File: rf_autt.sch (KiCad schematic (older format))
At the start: 10 parts

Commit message: PCB is Done... Needs DRC check
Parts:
- gave numbers to parts that had none: 10
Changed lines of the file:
@@
 $Descr A4 11693 8268
 encoding utf-8
-Sheet 7 14
+Sheet 7 7
 Title "HF-SDR RF-Attenuator"
 Date "2020 december"
@@
 OUT
 $Comp
-L sdr:FST3253 U?
+L sdr:FST3253 U4
 U 1 1 5FE50A6B
 P 5600 1900
-F 0 "U?" H 5350 2550 50  0000 C CNN
+F 0 "U4" H 5350 2550 50  0000 C CNN
 F 1 "FST3253" H 5800 2550 50  0000 C CNN
 F 2 "Package_SO:TSSOP-16_4.4x5mm_P0.65mm" H 5600 1900 50  0001 C CNN
@@
 ATT_SEL1
 $Comp
-L power:GNDA #PWR?
+L power:GNDA #PWR031
 U 1 1 5FE53082
 P 5600 4400
-F 0 "#PWR?" H 5600 4150 50  0001 C CNN
+F 0 "#PWR031" H 5600 4150 50  0001 C CNN
 F 1 "GNDA" H 5605 4227 50  0000 C CNN
 F 2 "" H 5600 4400 50  0001 C CNN
@@
 $EndComp
 $Comp
-L Device:R R?
+L Device:R R37
 U 1 1 5FE56E4E
 P 5600 4250
-F 0 "R?" H 5530 4204 50  0000 R CNN
+F 0 "R37" H 5530 4204 50  0000 R CNN
 F 1 "33" H 5530 4295 50  0000 R CNN
 F 2 "Resistor_SMD:R_0805_2012Metric_Pad1.20x1.40mm_HandSolder" V 5530 4250 50  0001 C CNN
@@
 $EndComp
 $Comp
-L Device:R R?
+L Device:R R24
 U 1 1 5FE5744A
 P 5300 3950
-F 0 "R?" V 5093 3950 50  0000 C CNN
+F 0 "R24" V 5093 3950 50  0000 C CNN
 F 1 "27" V 5184 3950 50  0000 C CNN
 F 2 "Resistor_SMD:R_0805_2012Metric_Pad1.20x1.40mm_HandSolder" V 5230 3950 50  0001 C CNN
@@
 $EndComp
 $Comp
-L Device:R R?
+L Device:R R40
 U 1 1 5FE57E99
 P 5900 3950
-F 0 "R?" V 5693 3950 50  0000 C CNN
+F 0 "R40" V 5693 3950 50  0000 C CNN
 F 1 "27" V 5784 3950 50  0000 C CNN
 F 2 "Resistor_SMD:R_0805_2012Metric_Pad1.20x1.40mm_HandSolder" V 5830 3950 50  0001 C CNN
@@
 	5600 3950 5750 3950
 $Comp
-L power:GNDA #PWR?
+L power:GNDA #PWR033
 U 1 1 5FE5C53B
 P 5600 6600
-F 0 "#PWR?" H 5600 6350 50  0001 C CNN
+F 0 "#PWR033" H 5600 6350 50  0001 C CNN
 F 1 "GNDA" H 5605 6427 50  0000 C CNN
 F 2 "" H 5600 6600 50  0001 C CNN
@@
 $EndComp
 $Comp
-L Device:R R?
+L Device:R R39
 U 1 1 5FE5C541
 P 5600 6450
-F 0 "R?" H 5530 6404 50  0000 R CNN
+F 0 "R39" H 5530 6404 50  0000 R CNN
 F 1 "3" H 5530 6495 50  0000 R CNN
 F 2 "Resistor_SMD:R_0805_2012Metric_Pad1.20x1.40mm_HandSolder" V 5530 6450 50  0001 C CNN
@@
 $EndComp
 $Comp
-L Device:R R?
+L Device:R R36
 U 1 1 5FE5C547
 P 5300 6150
-F 0 "R?" V 5093 6150 50  0000 C CNN
+F 0 "R36" V 5093 6150 50  0000 C CNN
 F 1 "47" V 5184 6150 50  0000 C CNN
 F 2 "Resistor_SMD:R_0805_2012Metric_Pad1.20x1.40mm_HandSolder" V 5230 6150 50  0001 C CNN
@@
 $EndComp
 $Comp
-L Device:R R?
+L Device:R R42
 U 1 1 5FE5C54D
 P 5900 6150
-F 0 "R?" V 5693 6150 50  0000 C CNN
+F 0 "R42" V 5693 6150 50  0000 C CNN
 F 1 "47" V 5784 6150 50  0000 C CNN
 F 2 "Resistor_SMD:R_0805_2012Metric_Pad1.20x1.40mm_HandSolder" V 5830 6150 50  0001 C CNN
@@
 	5600 6150 5750 6150
 $Comp
-L power:GNDA #PWR?
+L power:GNDA #PWR032
 U 1 1 5FE5CA2D
 P 5600 5500
-F 0 "#PWR?" H 5600 5250 50  0001 C CNN
+F 0 "#PWR032" H 5600 5250 50  0001 C CNN
 F 1 "GNDA" H 5605 5327 50  0000 C CNN
 F 2 "" H 5600 5500 50  0001 C CNN
@@
 $EndComp
 $Comp
-L Device:R R?
+L Device:R R38
 U 1 1 5FE5CA33
 P 5600 5350
-F 0 "R?" H 5530 5304 50  0000 R CNN
+F 0 "R38" H 5530 5304 50  0000 R CNN
 F 1 "10" H 5530 5395 50  0000 R CNN
 F 2 "Resistor_SMD:R_0805_2012Metric_Pad1.20x1.40mm_HandSolder" V 5530 5350 50  0001 C CNN
@@
 $EndComp
 $Comp
-L Device:R R?
+L Device:R R35
 U 1 1 5FE5CA39
 P 5300 5050
-F 0 "R?" V 5093 5050 50  0000 C CNN
+F 0 "R35" V 5093 5050 50  0000 C CNN
 F 1 "39" V 5184 5050 50  0000 C CNN
 F 2 "Resistor_SMD:R_0805_2012Metric_Pad1.20x1.40mm_HandSolder" V 5230 5050 50  0001 C CNN
@@
 $EndComp
 $Comp
-L Device:R R?
+L Device:R R41
 U 1 1 5FE5CA3F
 P 5900 5050
-F 0 "R?" V 5693 5050 50  0000 C CNN
+F 0 "R41" V 5693 5050 50  0000 C CNN
 F 1 "39" V 5784 5050 50  0000 C CNN
 F 2 "Resistor_SMD:R_0805_2012Metric_Pad1.20x1.40mm_HandSolder" V 5830 5050 50  0001 C CNN
@@
 	4300 800  5100 800
 $Comp
-L power:GNDA #PWR?
+L power:GNDA #PWR030
 U 1 1 5FF9D7B5
 P 5600 2700
-F 0 "#PWR?" H 5600 2450 50  0001 C CNN
+F 0 "#PWR030" H 5600 2450 50  0001 C CNN
 F 1 "GNDA" H 5605 2527 50  0000 C CNN
 F 2 "" H 5600 2700 50  0001 C CNN
@@
 $EndComp
 $Comp
-L power:GNDA #PWR?
+L power:GNDA #PWR034
 U 1 1 5FF9DC72
 P 6300 1550
-F 0 "#PWR?" H 6300 1300 50  0001 C CNN
+F 0 "#PWR034" H 6300 1300 50  0001 C CNN
 F 1 "GNDA" H 6305 1377 50  0000 C CNN
 F 2 "" H 6300 1550 50  0001 C CNN
@@
 Connection ~ 6300 1550
 $Comp
-L power:+5VA #PWR?
+L power:+5VA #PWR029
 U 1 1 5FF9E701
 P 5600 1200
-F 0 "#PWR?" H 5600 1050 50  0001 C CNN
+F 0 "#PWR029" H 5600 1050 50  0001 C CNN
 F 1 "+5VA" H 5615 1373 50  0000 C CNN
 F 2 "" H 5600 1200 50  0001 C CNN

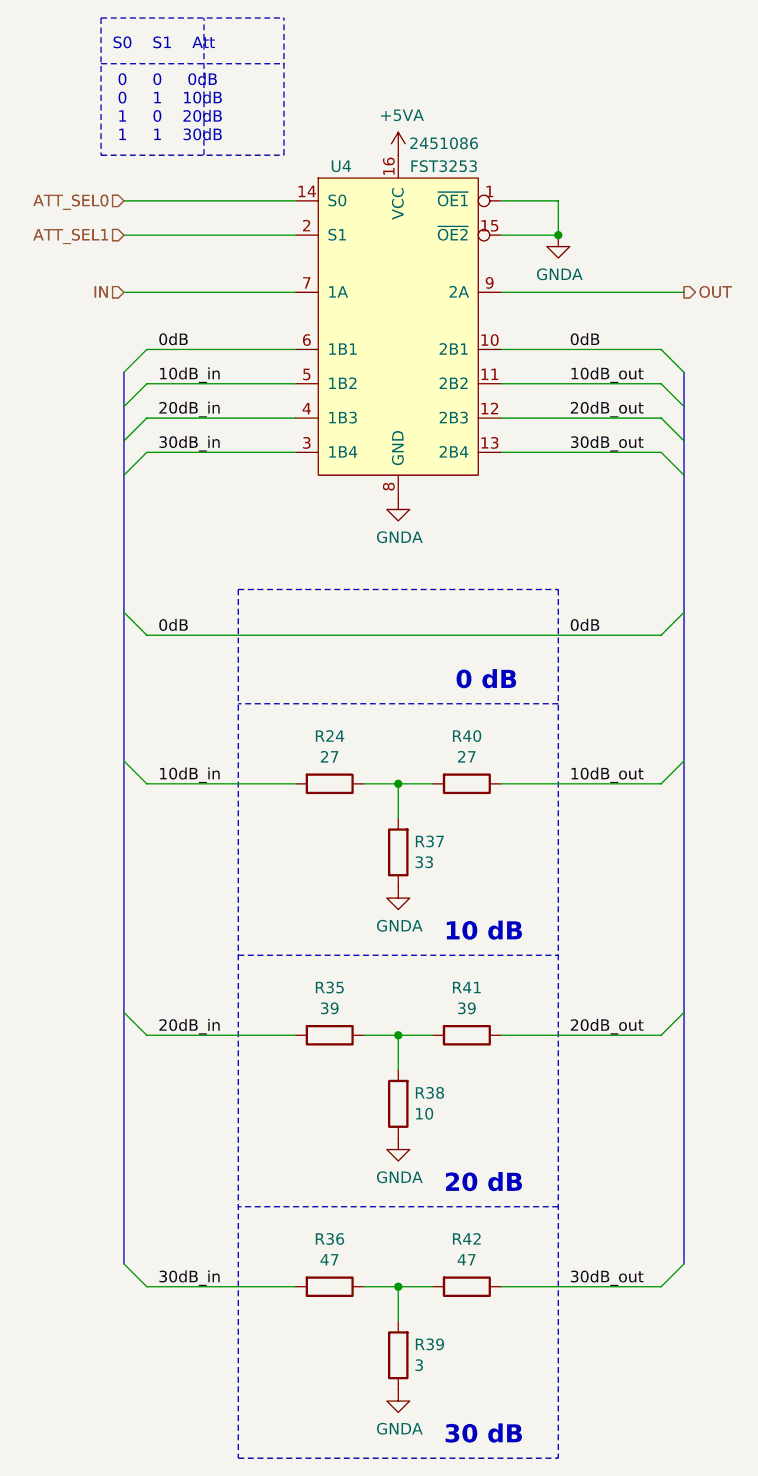
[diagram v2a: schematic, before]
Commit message: RX PCB revision: Diff amp + Mixer2
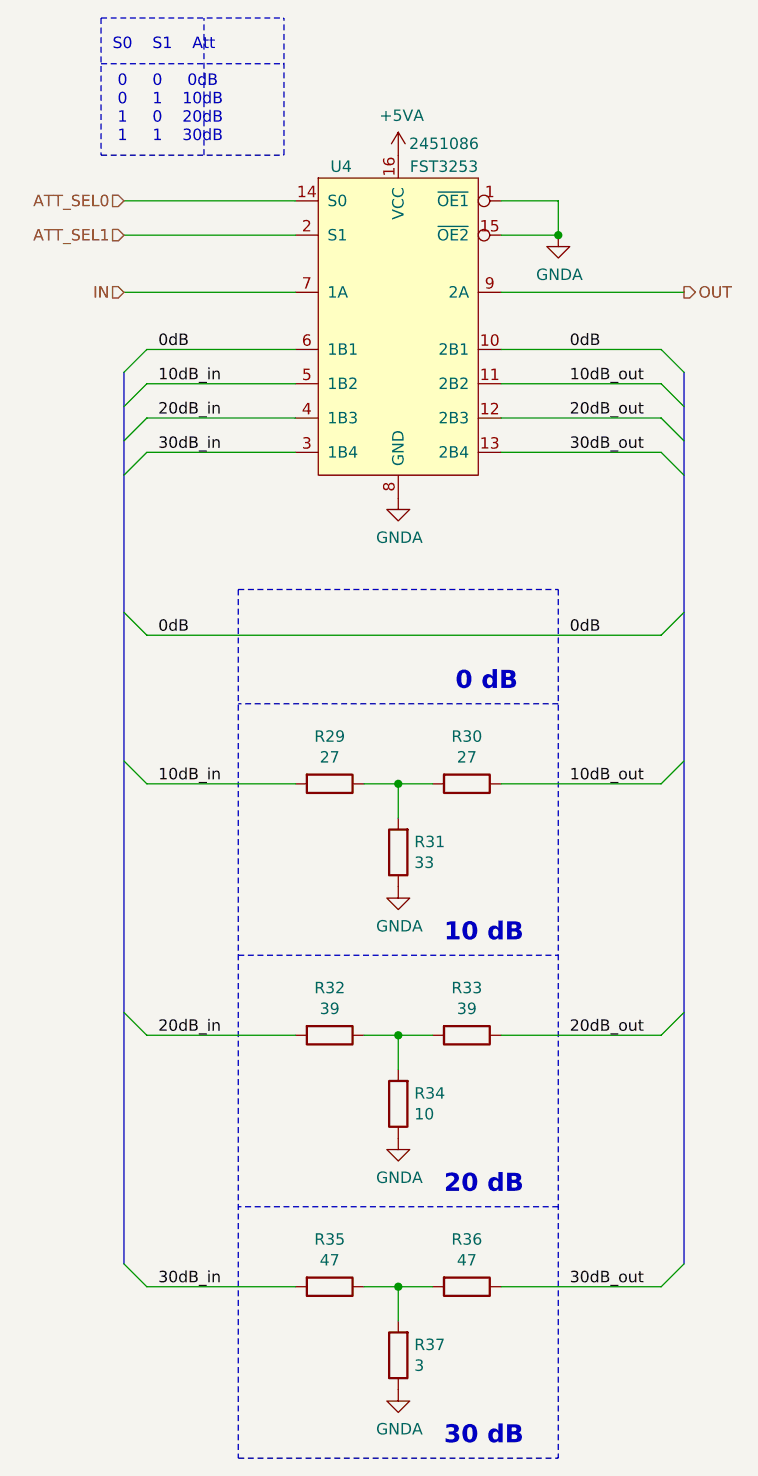
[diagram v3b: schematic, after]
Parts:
- R29: renamed from R24; footprint Resistor_SMD:R_0805_2012Metric_Pad1.20x1.40mm_HandSolder -> Resistor_SMD:R_0805_2012Metric_Pad1.15x1.40mm_HandSolder
- R30: renamed from R40; footprint Resistor_SMD:R_0805_2012Metric_Pad1.20x1.40mm_HandSolder -> Resistor_SMD:R_0805_2012Metric_Pad1.15x1.40mm_HandSolder
- R31: renamed from R37; footprint Resistor_SMD:R_0805_2012Metric_Pad1.20x1.40mm_HandSolder -> Resistor_SMD:R_0805_2012Metric_Pad1.15x1.40mm_HandSolder
- R32: renamed from R35; footprint Resistor_SMD:R_0805_2012Metric_Pad1.20x1.40mm_HandSolder -> Resistor_SMD:R_0805_2012Metric_Pad1.15x1.40mm_HandSolder
- R33: renamed from R41; footprint Resistor_SMD:R_0805_2012Metric_Pad1.20x1.40mm_HandSolder -> Resistor_SMD:R_0805_2012Metric_Pad1.15x1.40mm_HandSolder
- R34: renamed from R38; footprint Resistor_SMD:R_0805_2012Metric_Pad1.20x1.40mm_HandSolder -> Resistor_SMD:R_0805_2012Metric_Pad1.15x1.40mm_HandSolder
- R35: renamed from R36; footprint Resistor_SMD:R_0805_2012Metric_Pad1.20x1.40mm_HandSolder -> Resistor_SMD:R_0805_2012Metric_Pad1.15x1.40mm_HandSolder
- R36: renamed from R42; footprint Resistor_SMD:R_0805_2012Metric_Pad1.20x1.40mm_HandSolder -> Resistor_SMD:R_0805_2012Metric_Pad1.15x1.40mm_HandSolder
- R37: renamed from R39; footprint Resistor_SMD:R_0805_2012Metric_Pad1.20x1.40mm_HandSolder -> Resistor_SMD:R_0805_2012Metric_Pad1.15x1.40mm_HandSolder
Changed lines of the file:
@@
 ATT_SEL1
 $Comp
-L power:GNDA #PWR031
+L power:GNDA #PWR045
 U 1 1 5FE53082
 P 5600 4400
-F 0 "#PWR031" H 5600 4150 50  0001 C CNN
+F 0 "#PWR045" H 5600 4150 50  0001 C CNN
 F 1 "GNDA" H 5605 4227 50  0000 C CNN
 F 2 "" H 5600 4400 50  0001 C CNN
@@
 $EndComp
 $Comp
-L Device:R R37
+L Device:R R31
 U 1 1 5FE56E4E
 P 5600 4250
-F 0 "R37" H 5530 4204 50  0000 R CNN
+F 0 "R31" H 5530 4204 50  0000 R CNN
 F 1 "33" H 5530 4295 50  0000 R CNN
-F 2 "Resistor_SMD:R_0805_2012Metric_Pad1.20x1.40mm_HandSolder" V 5530 4250 50  0001 C CNN
+F 2 "Resistor_SMD:R_0805_2012Metric_Pad1.15x1.40mm_HandSolder" V 5530 4250 50  0001 C CNN
 F 3 "~" H 5600 4250 50  0001 C CNN
 	1    5600 4250
@@
 $EndComp
 $Comp
-L Device:R R24
+L Device:R R29
 U 1 1 5FE5744A
 P 5300 3950
-F 0 "R24" V 5093 3950 50  0000 C CNN
+F 0 "R29" V 5093 3950 50  0000 C CNN
 F 1 "27" V 5184 3950 50  0000 C CNN
-F 2 "Resistor_SMD:R_0805_2012Metric_Pad1.20x1.40mm_HandSolder" V 5230 3950 50  0001 C CNN
+F 2 "Resistor_SMD:R_0805_2012Metric_Pad1.15x1.40mm_HandSolder" V 5230 3950 50  0001 C CNN
 F 3 "~" H 5300 3950 50  0001 C CNN
 	1    5300 3950
@@
 $EndComp
 $Comp
-L Device:R R40
+L Device:R R30
 U 1 1 5FE57E99
 P 5900 3950
-F 0 "R40" V 5693 3950 50  0000 C CNN
+F 0 "R30" V 5693 3950 50  0000 C CNN
 F 1 "27" V 5784 3950 50  0000 C CNN
-F 2 "Resistor_SMD:R_0805_2012Metric_Pad1.20x1.40mm_HandSolder" V 5830 3950 50  0001 C CNN
+F 2 "Resistor_SMD:R_0805_2012Metric_Pad1.15x1.40mm_HandSolder" V 5830 3950 50  0001 C CNN
 F 3 "~" H 5900 3950 50  0001 C CNN
 	1    5900 3950
@@
 	5600 3950 5750 3950
 $Comp
-L power:GNDA #PWR033
+L power:GNDA #PWR047
 U 1 1 5FE5C53B
 P 5600 6600
-F 0 "#PWR033" H 5600 6350 50  0001 C CNN
+F 0 "#PWR047" H 5600 6350 50  0001 C CNN
 F 1 "GNDA" H 5605 6427 50  0000 C CNN
 F 2 "" H 5600 6600 50  0001 C CNN
@@
 $EndComp
 $Comp
-L Device:R R39
+L Device:R R37
 U 1 1 5FE5C541
 P 5600 6450
-F 0 "R39" H 5530 6404 50  0000 R CNN
+F 0 "R37" H 5530 6404 50  0000 R CNN
 F 1 "3" H 5530 6495 50  0000 R CNN
-F 2 "Resistor_SMD:R_0805_2012Metric_Pad1.20x1.40mm_HandSolder" V 5530 6450 50  0001 C CNN
+F 2 "Resistor_SMD:R_0805_2012Metric_Pad1.15x1.40mm_HandSolder" V 5530 6450 50  0001 C CNN
 F 3 "~" H 5600 6450 50  0001 C CNN
 	1    5600 6450
@@
 $EndComp
 $Comp
-L Device:R R36
+L Device:R R35
 U 1 1 5FE5C547
 P 5300 6150
-F 0 "R36" V 5093 6150 50  0000 C CNN
+F 0 "R35" V 5093 6150 50  0000 C CNN
 F 1 "47" V 5184 6150 50  0000 C CNN
-F 2 "Resistor_SMD:R_0805_2012Metric_Pad1.20x1.40mm_HandSolder" V 5230 6150 50  0001 C CNN
+F 2 "Resistor_SMD:R_0805_2012Metric_Pad1.15x1.40mm_HandSolder" V 5230 6150 50  0001 C CNN
 F 3 "~" H 5300 6150 50  0001 C CNN
 	1    5300 6150
@@
 $EndComp
 $Comp
-L Device:R R42
+L Device:R R36
 U 1 1 5FE5C54D
 P 5900 6150
-F 0 "R42" V 5693 6150 50  0000 C CNN
+F 0 "R36" V 5693 6150 50  0000 C CNN
 F 1 "47" V 5784 6150 50  0000 C CNN
-F 2 "Resistor_SMD:R_0805_2012Metric_Pad1.20x1.40mm_HandSolder" V 5830 6150 50  0001 C CNN
+F 2 "Resistor_SMD:R_0805_2012Metric_Pad1.15x1.40mm_HandSolder" V 5830 6150 50  0001 C CNN
 F 3 "~" H 5900 6150 50  0001 C CNN
 	1    5900 6150
@@
 	5600 6150 5750 6150
 $Comp
-L power:GNDA #PWR032
+L power:GNDA #PWR046
 U 1 1 5FE5CA2D
 P 5600 5500
-F 0 "#PWR032" H 5600 5250 50  0001 C CNN
+F 0 "#PWR046" H 5600 5250 50  0001 C CNN
 F 1 "GNDA" H 5605 5327 50  0000 C CNN
 F 2 "" H 5600 5500 50  0001 C CNN
@@
 $EndComp
 $Comp
-L Device:R R38
+L Device:R R34
 U 1 1 5FE5CA33
 P 5600 5350
-F 0 "R38" H 5530 5304 50  0000 R CNN
+F 0 "R34" H 5530 5304 50  0000 R CNN
 F 1 "10" H 5530 5395 50  0000 R CNN
-F 2 "Resistor_SMD:R_0805_2012Metric_Pad1.20x1.40mm_HandSolder" V 5530 5350 50  0001 C CNN
+F 2 "Resistor_SMD:R_0805_2012Metric_Pad1.15x1.40mm_HandSolder" V 5530 5350 50  0001 C CNN
 F 3 "~" H 5600 5350 50  0001 C CNN
 	1    5600 5350
@@
 $EndComp
 $Comp
-L Device:R R35
+L Device:R R32
 U 1 1 5FE5CA39
 P 5300 5050
-F 0 "R35" V 5093 5050 50  0000 C CNN
+F 0 "R32" V 5093 5050 50  0000 C CNN
 F 1 "39" V 5184 5050 50  0000 C CNN
-F 2 "Resistor_SMD:R_0805_2012Metric_Pad1.20x1.40mm_HandSolder" V 5230 5050 50  0001 C CNN
+F 2 "Resistor_SMD:R_0805_2012Metric_Pad1.15x1.40mm_HandSolder" V 5230 5050 50  0001 C CNN
 F 3 "~" H 5300 5050 50  0001 C CNN
 	1    5300 5050
@@
 $EndComp
 $Comp
-L Device:R R41
+L Device:R R33
 U 1 1 5FE5CA3F
 P 5900 5050
-F 0 "R41" V 5693 5050 50  0000 C CNN
+F 0 "R33" V 5693 5050 50  0000 C CNN
 F 1 "39" V 5784 5050 50  0000 C CNN
-F 2 "Resistor_SMD:R_0805_2012Metric_Pad1.20x1.40mm_HandSolder" V 5830 5050 50  0001 C CNN
+F 2 "Resistor_SMD:R_0805_2012Metric_Pad1.15x1.40mm_HandSolder" V 5830 5050 50  0001 C CNN
 F 3 "~" H 5900 5050 50  0001 C CNN
 	1    5900 5050
@@
 	4300 800  5100 800
 $Comp
-L power:GNDA #PWR030
+L power:GNDA #PWR044
 U 1 1 5FF9D7B5
 P 5600 2700
-F 0 "#PWR030" H 5600 2450 50  0001 C CNN
+F 0 "#PWR044" H 5600 2450 50  0001 C CNN
 F 1 "GNDA" H 5605 2527 50  0000 C CNN
 F 2 "" H 5600 2700 50  0001 C CNN
@@
 $EndComp
 $Comp
-L power:GNDA #PWR034
+L power:GNDA #PWR043
 U 1 1 5FF9DC72
 P 6300 1550
-F 0 "#PWR034" H 6300 1300 50  0001 C CNN
+F 0 "#PWR043" H 6300 1300 50  0001 C CNN
 F 1 "GNDA" H 6305 1377 50  0000 C CNN
 F 2 "" H 6300 1550 50  0001 C CNN
@@
 Connection ~ 6300 1550
 $Comp
-L power:+5VA #PWR029
+L power:+5VA #PWR042
 U 1 1 5FF9E701
 P 5600 1200
-F 0 "#PWR029" H 5600 1050 50  0001 C CNN
+F 0 "#PWR042" H 5600 1050 50  0001 C CNN
 F 1 "+5VA" H 5615 1373 50  0000 C CNN
 F 2 "" H 5600 1200 50  0001 C CNN
